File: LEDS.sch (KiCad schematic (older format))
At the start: 98 parts, among them U203 74HC125D

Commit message: add cached symbols to local library
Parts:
- LED1, LED10, LED11, LED12, LED13, LED14, LED15, LED16, LED17, LED18, LED19, LED2, LED20, LED21, LED22, LED23, LED24, LED25, LED26, LED27, LED28, LED29, LED3, LED30, LED31, LED32, LED33, LED34, LED35, LED36, LED37, LED38, LED39, LED4, LED40, LED41, LED42, LED43, LED44, LED45, LED46, LED47, LED5, LED6, LED7, LED8, LED9: symbol OTTOdiy_SMD-rescue:NeoPixel_THT-LED -> OTTOdiy_SMD-library:NeoPixel_THT-LED
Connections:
- net +5V_MAIN: no longer LED1.2 (VDD), LED10.2 (VDD), LED11.2 (VDD), LED12.2 (VDD), LED13.2 (VDD), LED14.2 (VDD), LED15.2 (VDD), LED16.2 (VDD), LED17.2 (VDD), LED18.2 (VDD), LED19.2 (VDD), LED2.2 (VDD), LED20.2 (VDD), LED21.2 (VDD), LED22.2 (VDD), LED23.2 (VDD), LED24.2 (VDD), LED25.2 (VDD), LED27.2 (VDD), LED28.2 (VDD), LED29.2 (VDD), LED3.2 (VDD), LED30.2 (VDD), LED31.2 (VDD), LED32.2 (VDD), LED33.2 (VDD), LED34.2 (VDD), LED35.2 (VDD), LED38.2 (VDD), LED39.2 (VDD), LED4.2 (VDD), LED40.2 (VDD), LED41.2 (VDD), LED42.2 (VDD), LED43.2 (VDD), LED44.2 (VDD), LED45.2 (VDD), LED46.2 (VDD), LED47.2 (VDD), LED5.2 (VDD), LED6.2 (VDD), LED7.2 (VDD)
- net GND: no longer LED1.3 (GND), LED10.3 (GND), LED11.3 (GND), LED12.3 (GND), LED13.3 (GND), LED14.3 (GND), LED15.3 (GND), LED17.3 (GND), LED18.3 (GND), LED19.3 (GND), LED2.3 (GND), LED20.3 (GND), LED21.3 (GND), LED22.3 (GND), LED23.3 (GND), LED24.3 (GND), LED25.3 (GND), LED27.3 (GND), LED28.3 (GND), LED29.3 (GND), LED3.3 (GND), LED30.3 (GND), LED31.3 (GND), LED32.3 (GND), LED33.3 (GND), LED34.3 (GND), LED35.3 (GND), LED36.3 (GND), LED38.3 (GND), LED39.3 (GND), LED4.3 (GND), LED40.3 (GND), LED41.3 (GND), LED42.3 (GND), LED43.3 (GND), LED44.3 (GND), LED45.3 (GND), LED46.3 (GND), LED5.3 (GND), LED6.3 (GND), LED7.3 (GND), LED9.3 (GND)

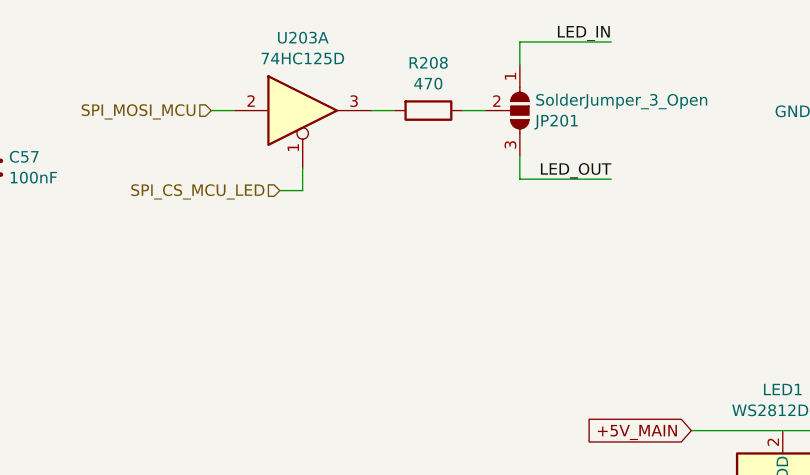
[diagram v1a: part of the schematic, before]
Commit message: PWR entry, ESD, JTAG, PU/PDs modified. Review pass 1
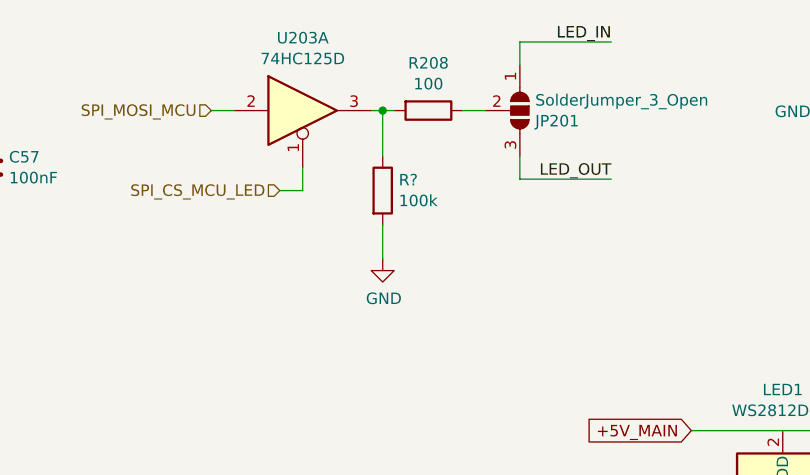
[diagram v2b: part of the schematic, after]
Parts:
- added R?: 100k, symbol Device:R
- R208: value 470 -> 100
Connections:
- net GND: now also R?.2
- net at R208.2, U203.3: now also R?.1
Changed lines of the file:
@@
 P 3700 1000
 F 0 "R208" V 3493 1000 50  0000 C CNN
-F 1 "470" V 3584 1000 50  0000 C CNN
+F 1 "100" V 3584 1000 50  0000 C CNN
 F 2 "Resistor_SMD:R_0805_2012Metric_Pad1.15x1.40mm_HandSolder" V 3630 1000 50  0001 C CNN
 F 3 "~" H 3700 1000 50  0001 C CNN
@@
 $EndComp
 Wire Wire Line
-	3450 1000 3550 1000
+	3450 1000 3500 1000
 Text HLabel 3050 1350 0    50   Input ~ 0
 SPI_CS_MCU_LED
@@
 Wire Wire Line
 	4850 2400 10150 2400
+$Comp
+L Device:R R?
+U 1 1 5E2E14CF
+P 3500 1350
+F 0 "R?" H 3570 1396 50  0000 L CNN
+F 1 "100k" H 3570 1305 50  0000 L CNN
+F 2 "" V 3430 1350 50  0001 C CNN
+F 3 "~" H 3500 1350 50  0001 C CNN
+	1    3500 1350
+	1    0    0    -1
+$EndComp
+$Comp
+L power:GND #PWR?
+U 1 1 5E2E1B34
+P 3500 1650
+F 0 "#PWR?" H 3500 1400 50  0001 C CNN
+F 1 "GND" H 3505 1477 50  0000 C CNN
+F 2 "" H 3500 1650 50  0001 C CNN
+F 3 "" H 3500 1650 50  0001 C CNN
+	1    3500 1650
+	1    0    0    -1
+$EndComp
+Wire Wire Line
+	3500 1500 3500 1650
+Wire Wire Line
+	3500 1200 3500 1000
+Connection ~ 3500 1000
+Wire Wire Line
+	3500 1000 3550 1000
 $EndSCHEMATC
